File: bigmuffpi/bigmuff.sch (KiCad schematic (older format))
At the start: 62 parts, among them J1 PWR JACK, J4 OUTPUT, J5 INPUT, Q1 BC239, Q2 BC239, Q3 BC239, Q4 BC239, SW1 POWER

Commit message: fix: update capacitors to the Film one
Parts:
- C10: footprint Capacitor_THT:C_Disc_D4.7mm_W2.5mm_P5.00mm -> Capacitor_THT:C_Rect_L7.2mm_W4.5mm_P5.00mm_FKS2_FKP2_MKS2_MKP2; Mfr. No K392K15X7RF53L2 -> FKP2C013901D00HC00; Mouser 594-K392K15X7RF53L2 -> 505-FKP2C013901DHC00
- C11: footprint Capacitor_THT:C_Disc_D4.7mm_W2.5mm_P5.00mm -> Capacitor_THT:C_Rect_L7.2mm_W5.5mm_P5.00mm_FKS2_FKP2_MKS2_MKP2; Mfr. No K103K15X7RH5TH5 -> FKP2C021001G00KSSD; Mouser 594-K103K15X7RH5TH5 -> 505-FKP2C021001G00KS
- C12, C13, C4, C7: footprint Capacitor_THT:C_Disc_D4.7mm_W2.5mm_P5.00mm -> Capacitor_THT:C_Rect_L7.2mm_W2.5mm_P5.00mm_FKS2_FKP2_MKS2_MKP2; Mfr. No K104K15X7RF53H5 -> B32529C104K000; Mouser 594-K104K15X7RF53H5 -> 871-B32529C104K000
- C2, C6, C9: footprint Capacitor_THT:C_Disc_D4.7mm_W2.5mm_P5.00mm -> Capacitor_THT:C_Rect_L7.2mm_W4.5mm_P5.00mm_FKS2_FKP2_MKS2_MKP2; Mfr. No K471K15X7RF53H5 -> FKP2D004701D00KSSD; Mouser 594-K471K15X7RF53H5 -> 505-FKP2D004701DKSSD
- C3: footprint Capacitor_THT:C_Disc_D4.7mm_W2.5mm_P5.00mm -> Capacitor_THT:C_Rect_L7.2mm_W5.5mm_P5.00mm_FKS2_FKP2_MKS2_MKP2; Mfr. No FG28X5R1H105KRT00 -> MKS2C041001F00KI00; Mouser 810-FG28X5R1H105KRT0 -> 505-MKS2C041001FKI00
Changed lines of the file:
@@
 F 0 "C2" V 2448 3300 50  0000 C CNN
 F 1 "470pF" V 2539 3300 50  0000 C CNN
-F 2 "Capacitor_THT:C_Disc_D4.7mm_W2.5mm_P5.00mm" H 2738 3150 50  0001 C CNN
-F 3 "https://cz.mouser.com/datasheet/2/427/kseries-1763315.pdf" H 2700 3300 50  0001 C CNN
-F 4 "K471K15X7RF53H5" H 2700 3300 50  0001 C CNN "Mfr. No"
-F 5 "594-K471K15X7RF53H5" H 2700 3300 50  0001 C CNN "Mouser"
+F 2 "Capacitor_THT:C_Rect_L7.2mm_W4.5mm_P5.00mm_FKS2_FKP2_MKS2_MKP2" H 2738 3150 50  0001 C CNN
+F 3 "https://cz.mouser.com/datasheet/2/440/e_WIMA_FKP_2-1139852.pdf" H 2700 3300 50  0001 C CNN
+F 4 "FKP2D004701D00KSSD " H 2700 3300 50  0001 C CNN "Mfr. No"
+F 5 "505-FKP2D004701DKSSD " H 2700 3300 50  0001 C CNN "Mouser"
 F 6 "Mouser" H 2700 3300 50  0001 C CNN "Supplier"
 	1    2700 3300
@@
 F 0 "C3" V 3452 3550 50  0000 C CNN
 F 1 "1uF" V 3361 3550 50  0000 C CNN
-F 2 "Capacitor_THT:C_Disc_D4.7mm_W2.5mm_P5.00mm" H 3238 3400 50  0001 C CNN
-F 3 "https://product.tdk.com/info/en/catalog/datasheets/leadmlcc_halogenfree_fg_en.pdf" H 3200 3550 50  0001 C CNN
-F 4 "FG28X5R1H105KRT00" H 3200 3550 50  0001 C CNN "Mfr. No"
-F 5 "810-FG28X5R1H105KRT0" H 3200 3550 50  0001 C CNN "Mouser"
+F 2 "Capacitor_THT:C_Rect_L7.2mm_W5.5mm_P5.00mm_FKS2_FKP2_MKS2_MKP2" H 3238 3400 50  0001 C CNN
+F 3 "https://cz.mouser.com/datasheet/2/440/e_WIMA_MKS_2-1139871.pdf" H 3200 3550 50  0001 C CNN
+F 4 "MKS2C041001F00KI00" H 3200 3550 50  0001 C CNN "Mfr. No"
+F 5 "505-MKS2C041001FKI00" H 3200 3550 50  0001 C CNN "Mouser"
 F 6 "Mouser" H 3200 3550 50  0001 C CNN "Supplier"
 	1    3200 3550
@@
 F 0 "C4" V 3598 3800 50  0000 C CNN
 F 1 "100nF" V 3689 3800 50  0000 C CNN
-F 2 "Capacitor_THT:C_Disc_D4.7mm_W2.5mm_P5.00mm" H 3888 3650 50  0001 C CNN
-F 3 "https://cz.mouser.com/datasheet/2/427/kseries-1763315.pdf" H 3850 3800 50  0001 C CNN
-F 4 "K104K15X7RF53H5" H 3850 3800 50  0001 C CNN "Mfr. No"
-F 5 "594-K104K15X7RF53H5" H 3850 3800 50  0001 C CNN "Mouser"
+F 2 "Capacitor_THT:C_Rect_L7.2mm_W2.5mm_P5.00mm_FKS2_FKP2_MKS2_MKP2" H 3888 3650 50  0001 C CNN
+F 3 "https://www.tdk-electronics.tdk.com/inf/20/20/db/fc_2009/B32520_529.pdf" H 3850 3800 50  0001 C CNN
+F 4 "B32529C104K000" H 3850 3800 50  0001 C CNN "Mfr. No"
+F 5 "871-B32529C104K000" H 3850 3800 50  0001 C CNN "Mouser"
 F 6 "Mouser" H 3850 3800 50  0001 C CNN "Supplier"
 	1    3850 3800
@@
 F 0 "C6" V 4748 3150 50  0000 C CNN
 F 1 "470pF" V 4839 3150 50  0000 C CNN
-F 2 "Capacitor_THT:C_Disc_D4.7mm_W2.5mm_P5.00mm" H 5038 3000 50  0001 C CNN
-F 3 "https://cz.mouser.com/datasheet/2/427/kseries-1763315.pdf" H 5000 3150 50  0001 C CNN
-F 4 "K471K15X7RF53H5" H 5000 3150 50  0001 C CNN "Mfr. No"
-F 5 "594-K471K15X7RF53H5" H 5000 3150 50  0001 C CNN "Mouser"
+F 2 "Capacitor_THT:C_Rect_L7.2mm_W4.5mm_P5.00mm_FKS2_FKP2_MKS2_MKP2" H 5038 3000 50  0001 C CNN
+F 3 "https://cz.mouser.com/datasheet/2/440/e_WIMA_FKP_2-1139852.pdf" H 5000 3150 50  0001 C CNN
+F 4 "FKP2D004701D00KSSD " H 5000 3150 50  0001 C CNN "Mfr. No"
+F 5 "505-FKP2D004701DKSSD " H 5000 3150 50  0001 C CNN "Mouser"
 F 6 "Mouser" H 5000 3150 50  0001 C CNN "Supplier"
 	1    5000 3150
@@
 F 0 "C7" V 5350 3500 50  0000 C CNN
 F 1 "100nF" V 5450 3500 50  0000 C CNN
-F 2 "Capacitor_THT:C_Disc_D4.7mm_W2.5mm_P5.00mm" H 5638 3350 50  0001 C CNN
-F 3 "https://cz.mouser.com/datasheet/2/427/kseries-1763315.pdf" H 5600 3500 50  0001 C CNN
-F 4 "K104K15X7RF53H5" H 5600 3500 50  0001 C CNN "Mfr. No"
-F 5 "594-K104K15X7RF53H5" H 5600 3500 50  0001 C CNN "Mouser"
+F 2 "Capacitor_THT:C_Rect_L7.2mm_W2.5mm_P5.00mm_FKS2_FKP2_MKS2_MKP2" H 5638 3350 50  0001 C CNN
+F 3 "https://www.tdk-electronics.tdk.com/inf/20/20/db/fc_2009/B32520_529.pdf" H 5600 3500 50  0001 C CNN
+F 4 "B32529C104K000" H 5600 3500 50  0001 C CNN "Mfr. No"
+F 5 "871-B32529C104K000" H 5600 3500 50  0001 C CNN "Mouser"
 F 6 "Mouser" H 5600 3500 50  0001 C CNN "Supplier"
 	1    5600 3500
@@
 F 0 "C9" V 6598 3150 50  0000 C CNN
 F 1 "470pF" V 6689 3150 50  0000 C CNN
-F 2 "Capacitor_THT:C_Disc_D4.7mm_W2.5mm_P5.00mm" H 6888 3000 50  0001 C CNN
-F 3 "https://cz.mouser.com/datasheet/2/427/kseries-1763315.pdf" H 6850 3150 50  0001 C CNN
-F 4 "K471K15X7RF53H5" H 6850 3150 50  0001 C CNN "Mfr. No"
-F 5 "594-K471K15X7RF53H5" H 6850 3150 50  0001 C CNN "Mouser"
+F 2 "Capacitor_THT:C_Rect_L7.2mm_W4.5mm_P5.00mm_FKS2_FKP2_MKS2_MKP2" H 6888 3000 50  0001 C CNN
+F 3 "https://cz.mouser.com/datasheet/2/440/e_WIMA_FKP_2-1139852.pdf" H 6850 3150 50  0001 C CNN
+F 4 "FKP2D004701D00KSSD " H 6850 3150 50  0001 C CNN "Mfr. No"
+F 5 "505-FKP2D004701DKSSD " H 6850 3150 50  0001 C CNN "Mouser"
 F 6 "Mouser" H 6850 3150 50  0001 C CNN "Supplier"
 	1    6850 3150
@@
 F 0 "C10" V 7698 3300 50  0000 C CNN
 F 1 "3.9nF" V 7789 3300 50  0000 C CNN
-F 2 "Capacitor_THT:C_Disc_D4.7mm_W2.5mm_P5.00mm" H 7988 3150 50  0001 C CNN
-F 3 "https://cz.mouser.com/datasheet/2/427/kseries-1763315.pdf" H 7950 3300 50  0001 C CNN
-F 4 "K392K15X7RF53L2" H 7950 3300 50  0001 C CNN "Mfr. No"
-F 5 "594-K392K15X7RF53L2" H 7950 3300 50  0001 C CNN "Mouser"
+F 2 "Capacitor_THT:C_Rect_L7.2mm_W4.5mm_P5.00mm_FKS2_FKP2_MKS2_MKP2" H 7988 3150 50  0001 C CNN
+F 3 "https://cz.mouser.com/datasheet/2/440/e_WIMA_FKP_2-1139852.pdf" H 7950 3300 50  0001 C CNN
+F 4 "FKP2C013901D00HC00" H 7950 3300 50  0001 C CNN "Mfr. No"
+F 5 "505-FKP2C013901DHC00" H 7950 3300 50  0001 C CNN "Mouser"
 F 6 "Mouser" H 7950 3300 50  0001 C CNN "Supplier"
 	1    7950 3300
@@
 F 0 "C12" V 8548 3550 50  0000 C CNN
 F 1 "100nF" V 8639 3550 50  0000 C CNN
-F 2 "Capacitor_THT:C_Disc_D4.7mm_W2.5mm_P5.00mm" H 8838 3400 50  0001 C CNN
-F 3 "https://cz.mouser.com/datasheet/2/427/kseries-1763315.pdf" H 8800 3550 50  0001 C CNN
-F 4 "K104K15X7RF53H5" H 8800 3550 50  0001 C CNN "Mfr. No"
-F 5 "594-K104K15X7RF53H5" H 8800 3550 50  0001 C CNN "Mouser"
+F 2 "Capacitor_THT:C_Rect_L7.2mm_W2.5mm_P5.00mm_FKS2_FKP2_MKS2_MKP2" H 8838 3400 50  0001 C CNN
+F 3 "https://www.tdk-electronics.tdk.com/inf/20/20/db/fc_2009/B32520_529.pdf" H 8800 3550 50  0001 C CNN
+F 4 "B32529C104K000" H 8800 3550 50  0001 C CNN "Mfr. No"
+F 5 "871-B32529C104K000" H 8800 3550 50  0001 C CNN "Mouser"
 F 6 "Mouser" H 8800 3550 50  0001 C CNN "Supplier"
 	1    8800 3550
@@
 F 0 "C13" V 9450 3350 50  0000 C CNN
 F 1 "100nF" V 9550 3350 50  0000 C CNN
-F 2 "Capacitor_THT:C_Disc_D4.7mm_W2.5mm_P5.00mm" H 9738 3100 50  0001 C CNN
-F 3 "https://cz.mouser.com/datasheet/2/427/kseries-1763315.pdf" H 9700 3250 50  0001 C CNN
-F 4 "K104K15X7RF53H5" H 9700 3250 50  0001 C CNN "Mfr. No"
-F 5 "594-K104K15X7RF53H5" H 9700 3250 50  0001 C CNN "Mouser"
+F 2 "Capacitor_THT:C_Rect_L7.2mm_W2.5mm_P5.00mm_FKS2_FKP2_MKS2_MKP2" H 9738 3100 50  0001 C CNN
+F 3 "https://www.tdk-electronics.tdk.com/inf/20/20/db/fc_2009/B32520_529.pdf" H 9700 3250 50  0001 C CNN
+F 4 "B32529C104K000" H 9700 3250 50  0001 C CNN "Mfr. No"
+F 5 "871-B32529C104K000" H 9700 3250 50  0001 C CNN "Mouser"
 F 6 "Mouser" H 9700 3250 50  0001 C CNN "Supplier"
 	1    9700 3250
@@
 F 0 "C11" H 8315 4096 50  0000 L CNN
 F 1 "10nF" H 8315 4005 50  0000 L CNN
-F 2 "Capacitor_THT:C_Disc_D4.7mm_W2.5mm_P5.00mm" H 8238 3900 50  0001 C CNN
-F 3 "https://cz.mouser.com/datasheet/2/427/kseries-1763315.pdf" H 8200 4050 50  0001 C CNN
-F 4 "K103K15X7RH5TH5" H 8200 4050 50  0001 C CNN "Mfr. No"
-F 5 "594-K103K15X7RH5TH5" H 8200 4050 50  0001 C CNN "Mouser"
+F 2 "Capacitor_THT:C_Rect_L7.2mm_W5.5mm_P5.00mm_FKS2_FKP2_MKS2_MKP2" H 8238 3900 50  0001 C CNN
+F 3 "https://cz.mouser.com/datasheet/2/440/e_WIMA_FKP_2-1139852.pdf" H 8200 4050 50  0001 C CNN
+F 4 "FKP2C021001G00KSSD " H 8200 4050 50  0001 C CNN "Mfr. No"
+F 5 "505-FKP2C021001G00KS " H 8200 4050 50  0001 C CNN "Mouser"
 F 6 "Mouser" H 8200 4050 50  0001 C CNN "Supplier"
 	1    8200 4050

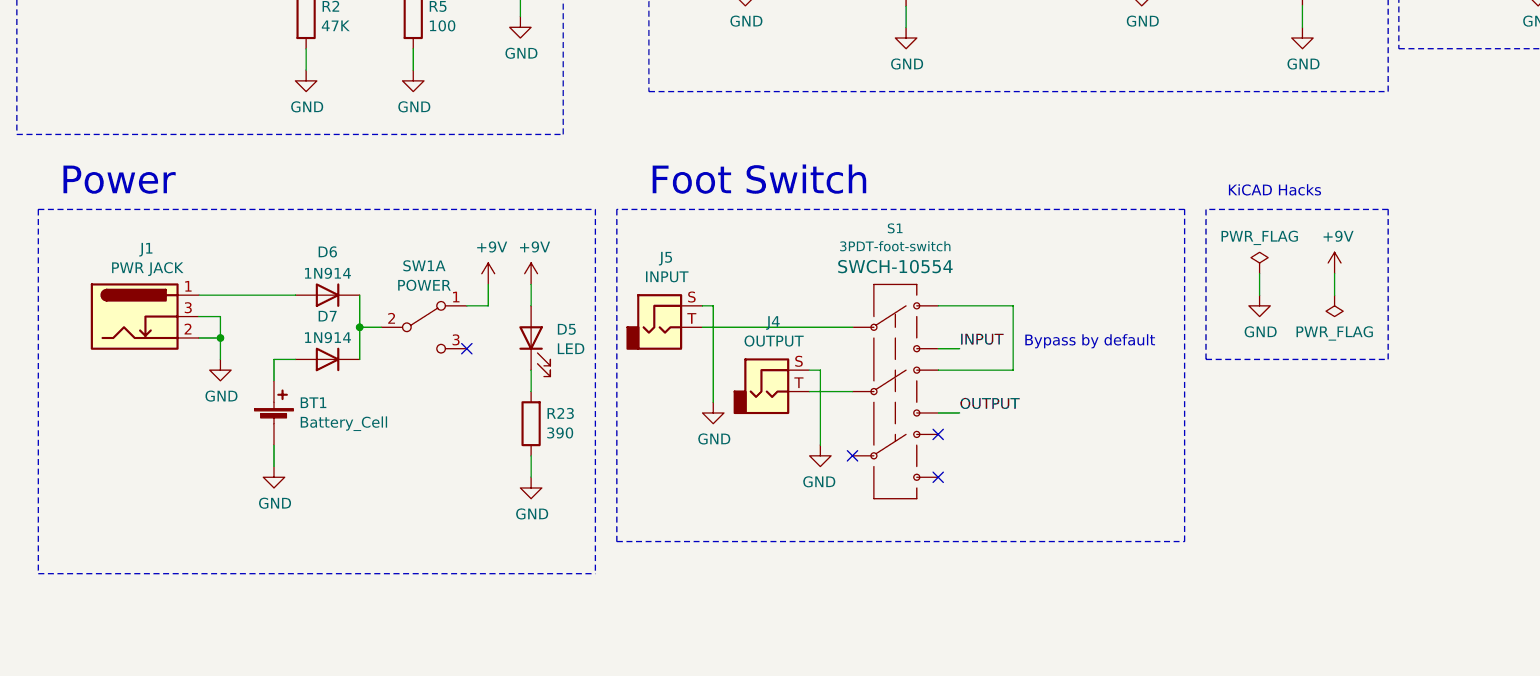
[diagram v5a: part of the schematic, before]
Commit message: fix: LED indicates effect
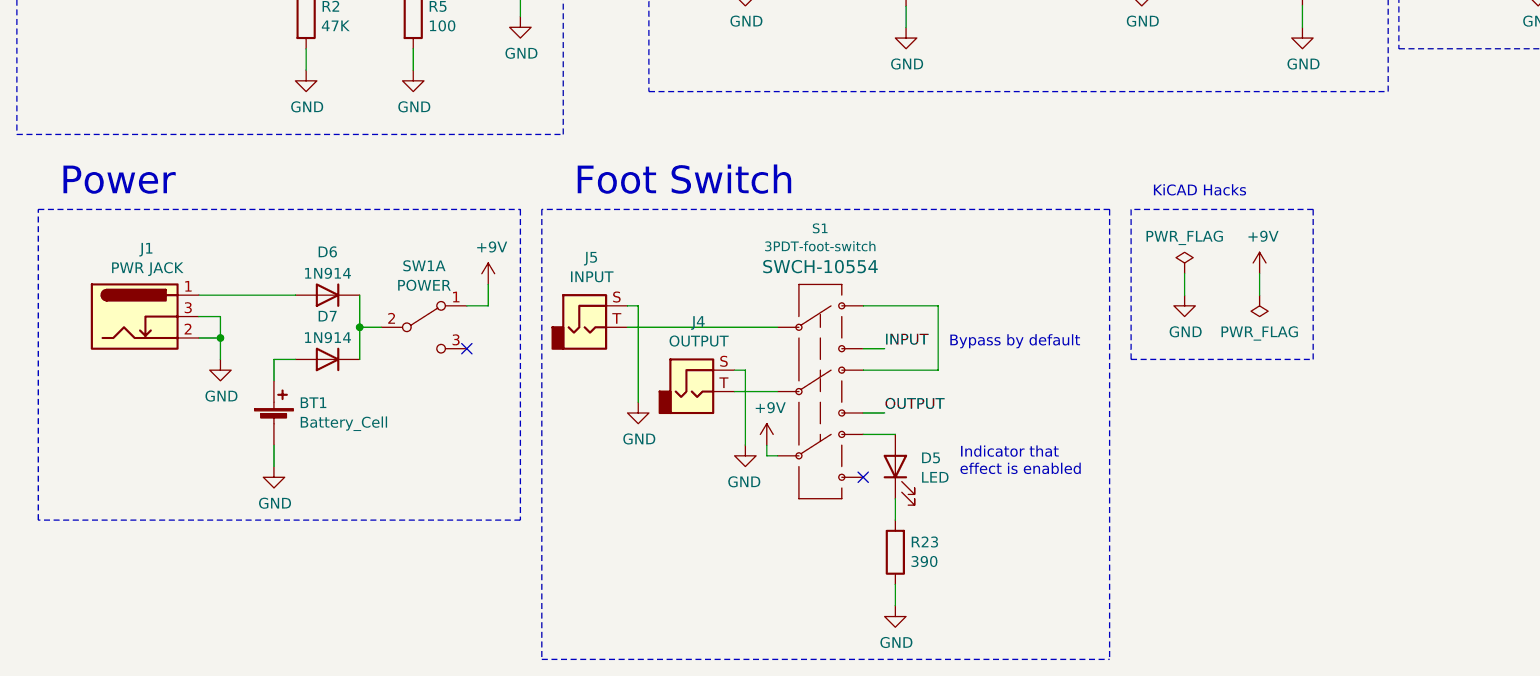
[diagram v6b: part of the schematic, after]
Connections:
- net +9V: now also S1.8; no longer D5.2 (A)
- net at S1.7: now also D5.2 (A)
- no-connect marks 4 -> 2
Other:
- note added: "Indicator that \neffect is enabled"
- moved on the sheet: D5, J4, J5, R23, S1
